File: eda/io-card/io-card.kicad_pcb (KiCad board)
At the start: 2 copper layers, 153 x 99.1 mm, 62 parts, among them J1 PS2, J2 Bus expansion, J3 PortA, J4 PortB, J5 ControlLines, J6 SPI, J7 Keyboard connector, J8 SD-Card module, J9 SD_Card, U1 W65C22SxP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

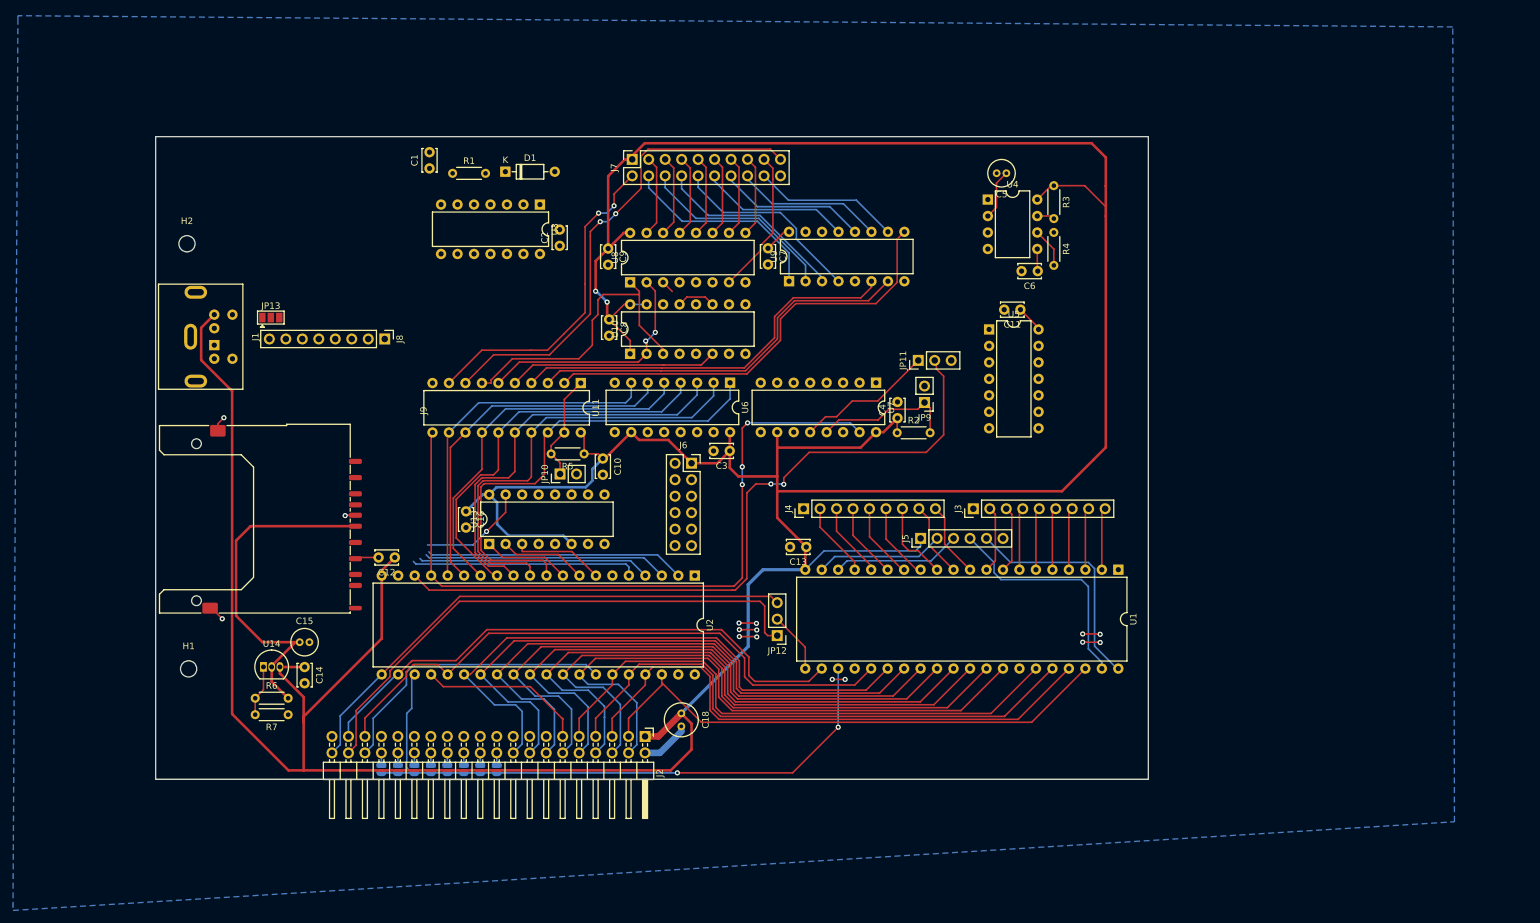
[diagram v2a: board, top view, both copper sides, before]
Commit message: EDA work for new expansion header
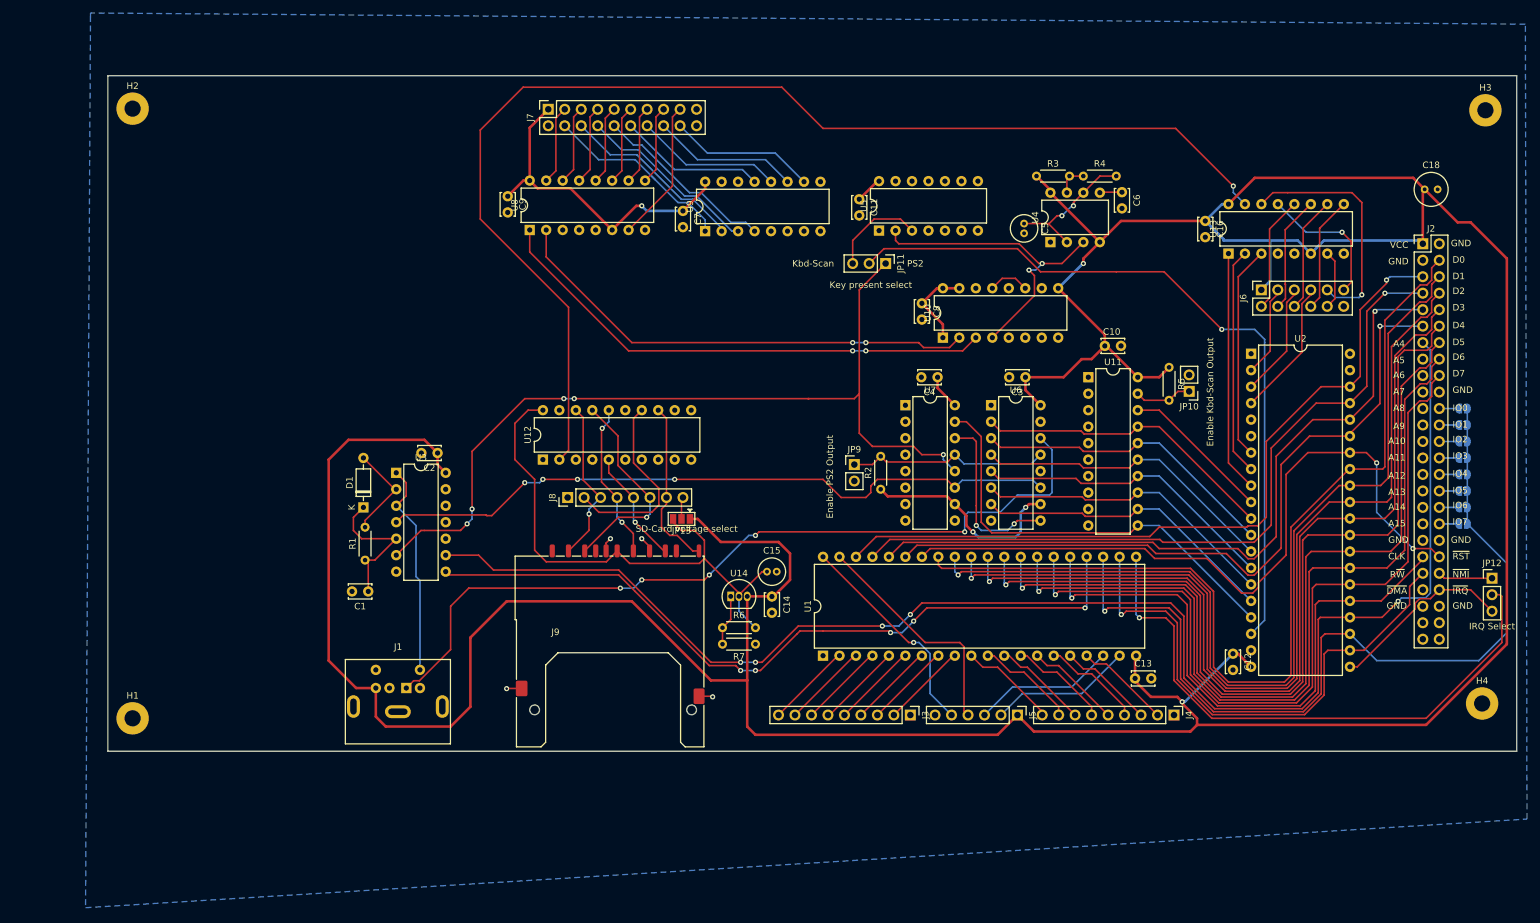
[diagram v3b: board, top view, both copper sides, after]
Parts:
- added H3: MountingHole_Pad, MountingHole:MountingHole_2.5mm_Pad, F.Cu at (242.6, 51.3)
- added H4: MountingHole_Pad, MountingHole:MountingHole_2.5mm_Pad, F.Cu at (242.1, 142.7)
- added U12: 74HC541, Package_DIP:DIP-20_W7.62mm, F.Cu at (97.3, 105.2)
- H1, H2: value MountingHole -> MountingHole_Pad; footprint MountingHole:MountingHole_2.5mm -> MountingHole:MountingHole_2.5mm_Pad
- J2: value Bus expansion -> Conn_02x25_Odd_Even; footprint Connector_PinHeader_2.54mm:PinHeader_2x20_P2.54mm_Horizontal -> Connector_PinHeader_2.54mm:PinHeader_2x25_P2.54mm_Vertical
- moved JP8 171.0 mm to (239.1, 115.1), turned to 0 degrees
- moved JP7 169.1 mm to (239.1, 112.5), turned to 0 degrees
- moved JP6 167.2 mm to (239.1, 110.0), turned to 0 degrees
- moved JP5 165.5 mm to (239.1, 107.4), turned to 0 degrees
- moved JP4 163.7 mm to (239.1, 104.9), turned to 0 degrees
- moved JP3 162.1 mm to (239.1, 102.4), turned to 0 degrees
- moved JP2 160.5 mm to (239.1, 99.8), turned to 0 degrees
- moved JP1 159.0 mm to (239.1, 97.3), turned to 0 degrees
- moved J2 141.9 mm to (232.9, 71.9), turned to 0 degrees
- moved C18 140.2 mm to (233.2, 63.5), turned to 0 degrees
- moved C12 130.1 mm to (203.7, 135.1), turned to -90 degrees
- moved U13 122.4 mm to (203.0, 73.4)
- moved C16 122.4 mm to (199.4, 68.4)
- moved JP12 110.5 mm to (243.6, 123.4), turned to 0 degrees
- moved JP10 97.8 mm to (196.9, 94.6), turned to 180 degrees
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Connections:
- J2 pad 11: /Expansion header/A4 -> /Expansion header/A3
- J2 pad 13: /Expansion header/A5 -> /Expansion header/A4
- J2 pad 15: /Expansion header/A6 -> /Expansion header/A5
- J2 pad 17: /Expansion header/A7 -> /Expansion header/A6
- J2 pad 19: /Expansion header/A8 -> /Expansion header/A7
- J2 pad 20: Net-(J2-Pin_20) -> GND
- J2 pad 21: /Expansion header/A9 -> /Expansion header/A8
- J2 pad 23: /Expansion header/A10 -> /Expansion header/A9
- J2 pad 25: /Expansion header/A11 -> /Expansion header/A10
- J2 pad 27: /Expansion header/A12 -> /Expansion header/A11
- J2 pad 29: /Expansion header/A13 -> /Expansion header/A12
- J2 pad 3: /Expansion header/A0 -> GND
- J2 pad 31: /Expansion header/A14 -> /Expansion header/A13
- J2 pad 33: /Expansion header/A15 -> /Expansion header/A14
- J2 pad 35: /Clock -> /Expansion header/A15
- J2 pad 36: /~{RST} -> Net-(J2-Pin_36)
- J2 pad 37: /R~{W} -> GND
- J2 pad 38: /~{NMI} -> GND
- J2 pad 39: /Expansion header/~{DMA} -> /Clock
- J2 pad 40: /~{IRQ} -> /~{RST}
- J2 pad 5: /Expansion header/A1 -> /Expansion header/A0
- J2 pad 7: /Expansion header/A2 -> /Expansion header/A1
- J2 pad 9: /Expansion header/A3 -> /Expansion header/A2
- J9 pad 1: unconnected-(J9-CD/DAT3-Pad1) -> /SD-Card/SD_CS
- J9 pad 2: unconnected-(J9-CMD-Pad2) -> /SD-Card/SD_SDO
- J9 pad 5: unconnected-(J9-CLK-Pad5) -> /SD-Card/SD_CLK
- JP1 pad 1: Net-(J2-Pin_20) -> Net-(J2-Pin_22)
- JP2 pad 1: Net-(J2-Pin_22) -> Net-(J2-Pin_24)
- JP3 pad 1: Net-(J2-Pin_24) -> Net-(J2-Pin_26)
- JP4 pad 1: Net-(J2-Pin_26) -> Net-(J2-Pin_28)
- JP5 pad 1: Net-(J2-Pin_28) -> Net-(J2-Pin_30)
- JP6 pad 1: Net-(J2-Pin_30) -> Net-(J2-Pin_32)
- JP7 pad 1: Net-(J2-Pin_32) -> Net-(J2-Pin_34)
- JP8 pad 1: Net-(J2-Pin_34) -> Net-(J2-Pin_36)
- U13 pad 15: /SD-Card/SD_CS -> /SD-Card/~{CS}
- U2 pad 6: /SD-Card/SD_WriteProtect -> /SD-Card/WriteProtect
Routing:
- net /Expansion header/A4: track 25.9 -> 227.8 mm, vias 0 -> 5
- net /SD-Card/~{CS}: track 0.00 -> 185.7 mm, vias 0 -> 1
- net /PS2 keyboard interface/KeyboardData: track 0.00 -> 126.5 mm, vias 0 -> 5
- net Net-(U1-CS1): track 0.00 -> 117.1 mm, vias 0 -> 5
- net /PS2 keyboard interface/KeyPresent: track 21.2 -> 133.4 mm, vias 0 -> 5
- net /PS2 keyboard interface/~{KeyboardClk}: track 0.00 -> 106.5 mm, vias 0 -> 4
- net Net-(JP12-C): track 9.41 -> 90.4 mm, vias 0 -> 1
- net /~{NMI}: track 84.0 -> 8.44 mm
- net /Scanning keyboard interface/mod1: track 74.5 -> 0.00 mm, vias 2 -> 0
- net VCC: track 636.1 -> 710.1 mm, vias 2 -> 5
- net /Scanning keyboard interface/Scancode3: track 67.9 -> 0.00 mm
- net /~{RST}: track 45.4 -> 110.9 mm, vias 0 -> 2
- net /Scanning keyboard interface/Scancode5: track 61.4 -> 0.00 mm
- net /Scanning keyboard interface/Scancode4: track 60.8 -> 0.00 mm
- net /Expansion header/D0: track 93.9 -> 147.5 mm
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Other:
- board size 153 x 99.1 mm -> 217.2 x 104.1 mm
- board text added: "A10"
- board text added: "A11"
- board text added: "A12"
- board text added: "A13"
- board text added: "A14"
- board text added: "A15"
- board text added: "A4"
- board text added: "A5"
- board text added: "A6"
- board text added: "A7"
- board text added: "A8"
- board text added: "A9"
- board text added: "CLK"
- board text added: "D0"
- board text added: "D1"
- board text added: "D2"
- board text added: "D3"
- board text added: "D4"
- board text added: "D5"
- board text added: "D6"
- board text added: "D7"
- board text added: "Enable Kbd-Scan Output"
- board text added: "GND"
- board text added: "IO0"
- board text added: "IO1"
- board text added: "IO2"
- board text added: "IO3"
- board text added: "IO4"
- board text added: "IO5"
- board text added: "IO6"
- board text added: "IO7"
- board text added: "J1"
- board text added: "Kbd-Scan"
- board text added: "PS2"
- board text added: "R~{W}"
- board text added: "VCC"
- board text added: "~{DMA}"
- board text added: "~{IRQ}"
- board text added: "~{NMI}"
- board text added: "~{RST}"

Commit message: Branch of uart to v1
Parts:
- removed U11: 74HCT541, Package_DIP:DIP-20_W7.62mm
- added U15: 74HCT574, Package_DIP:DIP-20_W7.62mm, F.Cu at (181.1, 92.5)
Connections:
- U5 pad 1: Net-(U9-GS) -> Net-(U9-EO)
- U9 pad 14: Net-(U9-GS) -> Net-(U15-Cp)
- U9 pad 15: unconnected-(U9-EO-Pad15) -> Net-(U9-EO)
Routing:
- net /SD-Card/WriteProtect: track 0.00 -> 97.6 mm, vias 0 -> 7
- net Net-(JP10-A): track 8.91 -> 3.67 mm
- net /PS2 keyboard interface/KeyboardBit1: track 47.2 -> 48.8 mm
- net /PS2 keyboard interface/KeyboardBit0: track 23.3 -> 24.6 mm
- net /PS2 keyboard interface/KeyboardBit6: track 47.2 -> 47.8 mm, vias 0 -> 1
- net /PS2 keyboard interface/KeyboardBit2: track 47.3 -> 47.0 mm, vias 0 -> 1
- net /PS2 keyboard interface/KeyboardBit5: track 47.2 -> 47.5 mm, vias 0 -> 1
- net /PS2 keyboard interface/KeyboardBit7: track 66.8 -> 67.1 mm, vias 0 -> 1
- net /PS2 keyboard interface/KeyboardBit4: vias 0 -> 1
- net /PS2 keyboard interface/KeyboardBit3: vias 0 -> 1

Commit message: Generate step files and start on gpu for new board layout
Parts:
- added H5: MountingHole_Pad, MountingHole:MountingHole_2.5mm_Pad_Via, F.Cu at (150.7, 51.9)
- added H6: MountingHole_Pad, MountingHole:MountingHole_2.5mm_Pad_Via, F.Cu at (150.9, 142.8)
- H1, H2, H3, H4: footprint MountingHole:MountingHole_2.5mm_Pad -> MountingHole:MountingHole_2.5mm_Pad_Via
- moved H1 94.2 mm to (20.6, 51.8)
- moved H2 92.7 mm to (20.6, 142.7)
- moved JP13 5.19 mm to (122.7, 111.0), turned to -90 degrees
- moved J9 2.45 mm to (108.1, 129.3)
- moved J1 2.19 mm to (76.2, 138.2)
- moved H3 1.00 mm to (241.7, 51.8)
- moved H4 0.35 mm to (241.7, 142.7)
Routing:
- net /SD-Card/SD_CardDetect: track 29.7 -> 40.6 mm
- net +3.3V: track 83.9 -> 91.2 mm
- net /SD-Card/SD_WriteProtect: track 26.2 -> 22.3 mm
- net Net-(J2-Pin_36): track 3.02 -> 6.32 mm
- net Net-(J2-Pin_34): track 3.02 -> 6.29 mm
- net Net-(J2-Pin_32): track 3.02 -> 6.29 mm
- net Net-(J2-Pin_30): track 3.02 -> 6.29 mm
- net Net-(J2-Pin_28): track 3.02 -> 6.29 mm
- net Net-(J2-Pin_26): track 3.02 -> 6.29 mm
- net Net-(J2-Pin_24): track 3.02 -> 6.29 mm
- net Net-(J2-Pin_22): track 3.02 -> 6.29 mm
- net /SD-Card/SD_CLK: track 24.2 -> 21.7 mm
- net Net-(J1-Pad5): track 33.2 -> 31.0 mm
- net /SD-Card/SD_CS: track 25.3 -> 23.8 mm
- net Net-(JP12-C): track 90.4 -> 89.0 mm
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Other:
- board size 217.2 x 104.1 mm -> 230 x 100 mm

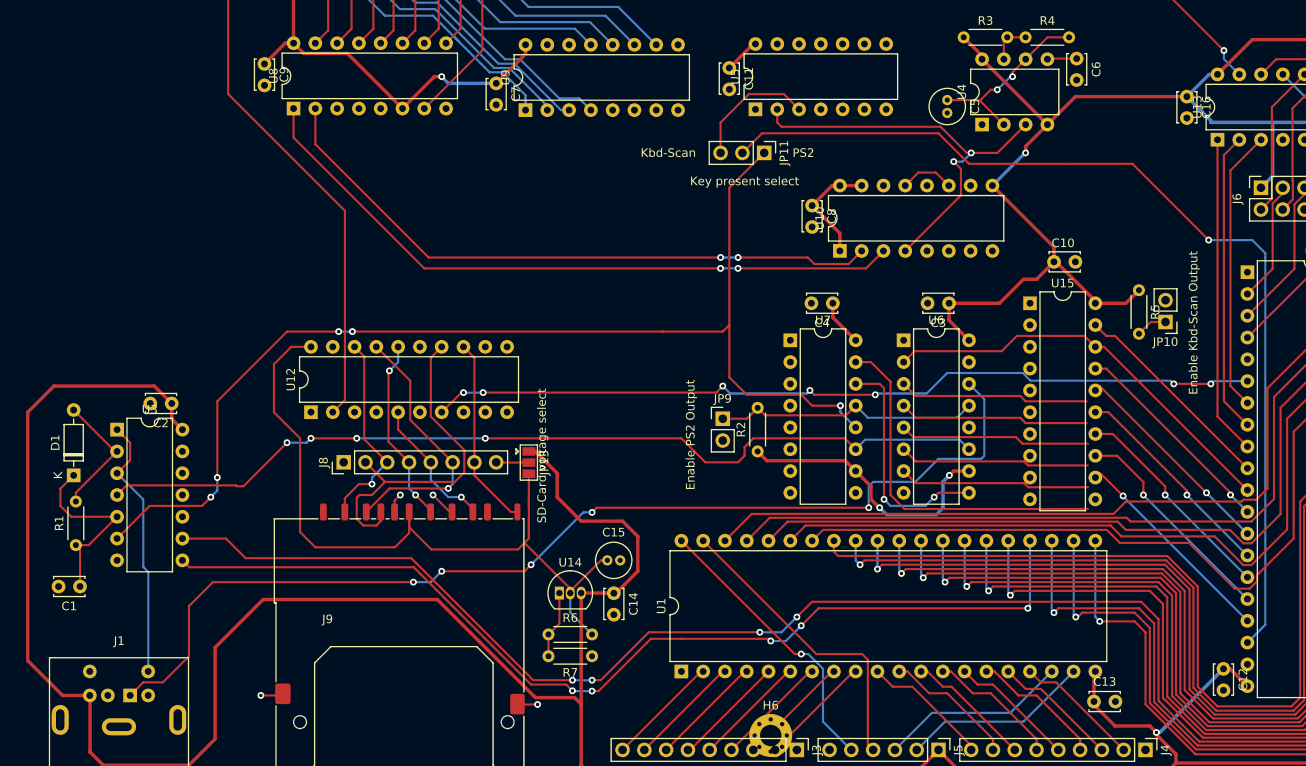
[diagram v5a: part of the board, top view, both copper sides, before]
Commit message: Normalize cap size
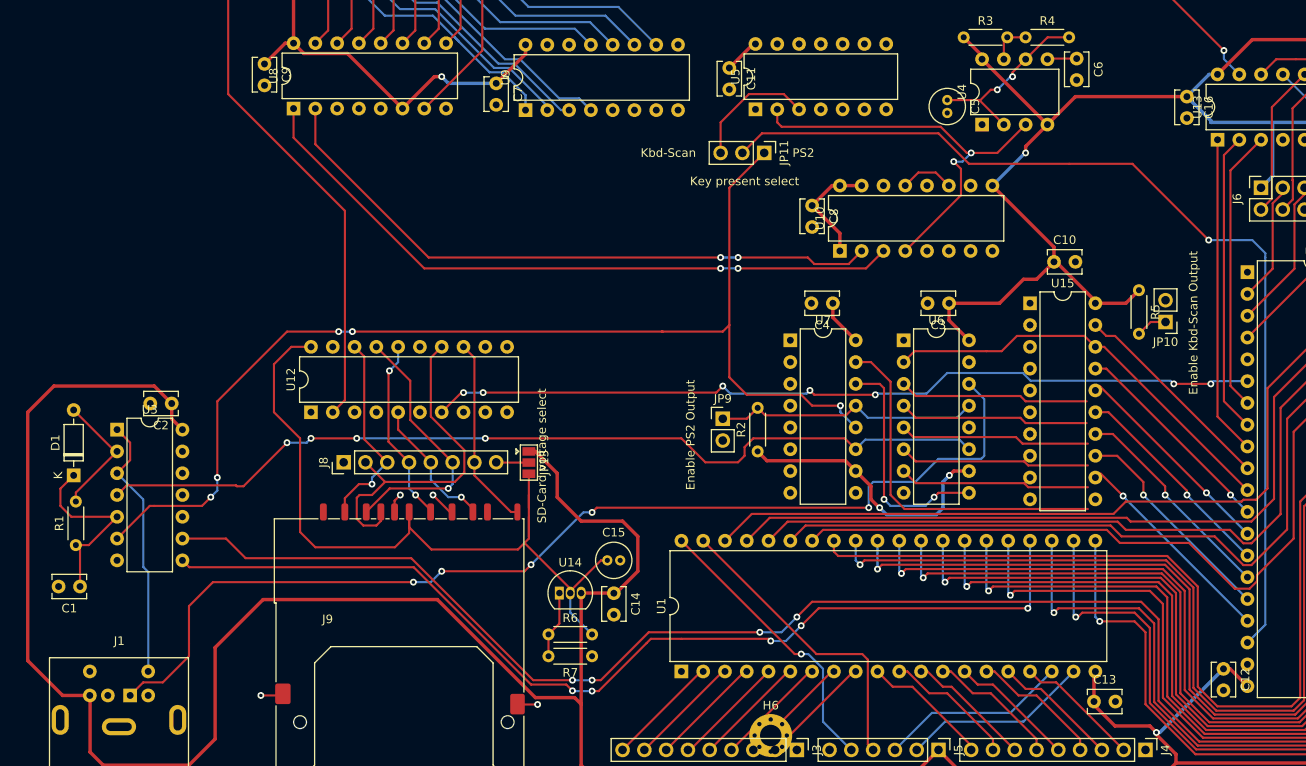
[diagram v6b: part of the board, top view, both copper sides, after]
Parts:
- C1, C10, C11, C12, C13, C14, C16, C2, C3, C4, C6, C7, C8, C9: footprint Capacitor_THT:C_Disc_D3.4mm_W2.1mm_P2.50mm -> Capacitor_THT:C_Disc_D3.8mm_W2.6mm_P2.50mm
